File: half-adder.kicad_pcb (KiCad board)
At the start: 2 copper layers, 100 x 100 mm, 55 parts, among them J1 A, J2 B, J3 C, J4 OUTPUT, J5 CARRY OUT, J6 5V, J7 GROUND, Q1 BC547, Q10 BC547, Q11 BC547, Q12 BC547, Q13 BC547, Q14 BC547, Q15 BC547, Q16 BC547, Q17 BC547, Q18 BC547, Q19 BC547, Q2 BC547, Q20 BC547, Q21 BC547, Q22 BC547, Q23 BC547, Q24 BC547, Q25 BC547, Q3 BC547, Q4 BC547, Q5 BC547, Q6 BC547, Q7 BC547, Q8 BC547, Q9 BC547

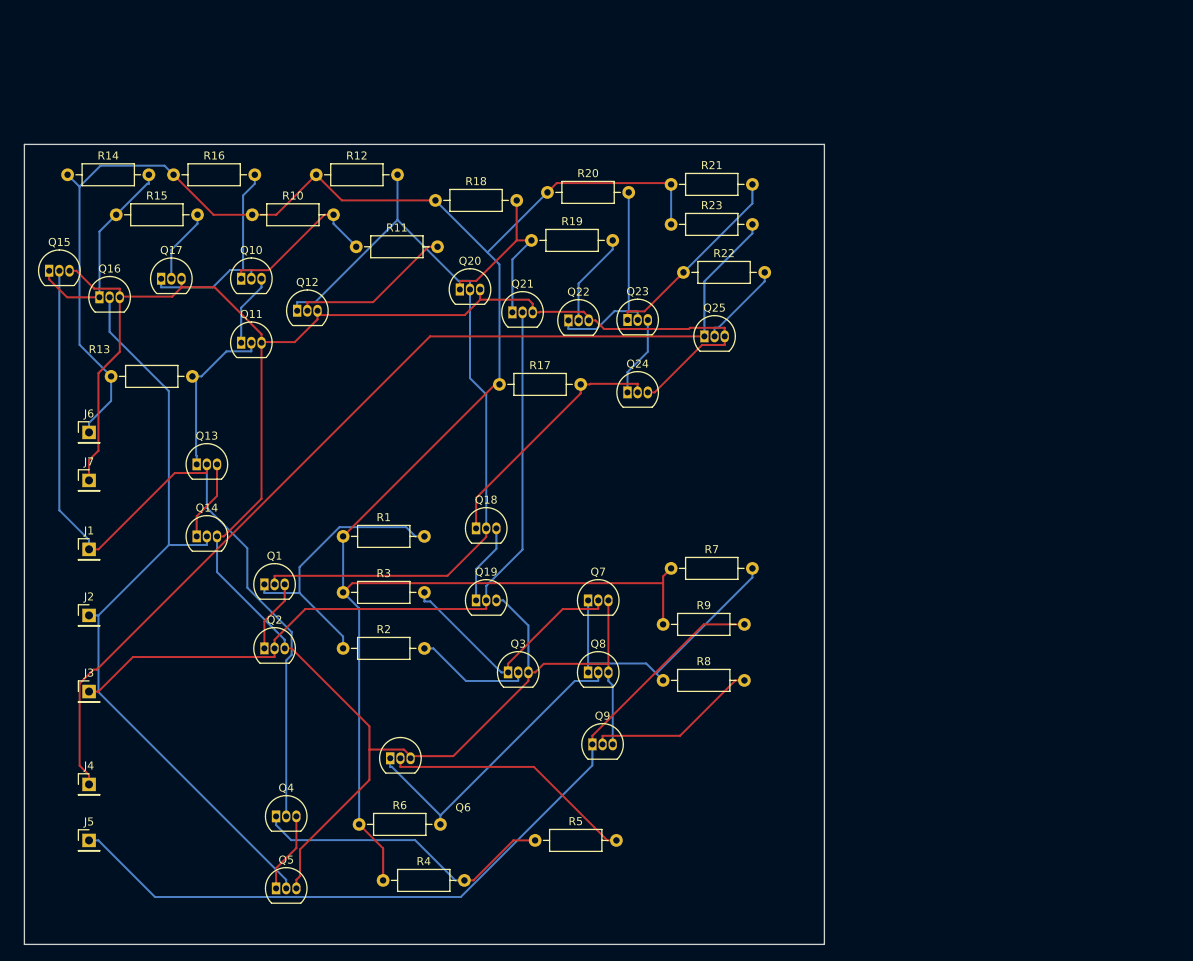
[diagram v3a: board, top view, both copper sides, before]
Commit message: Add ground plane to half adder and modularize or gate
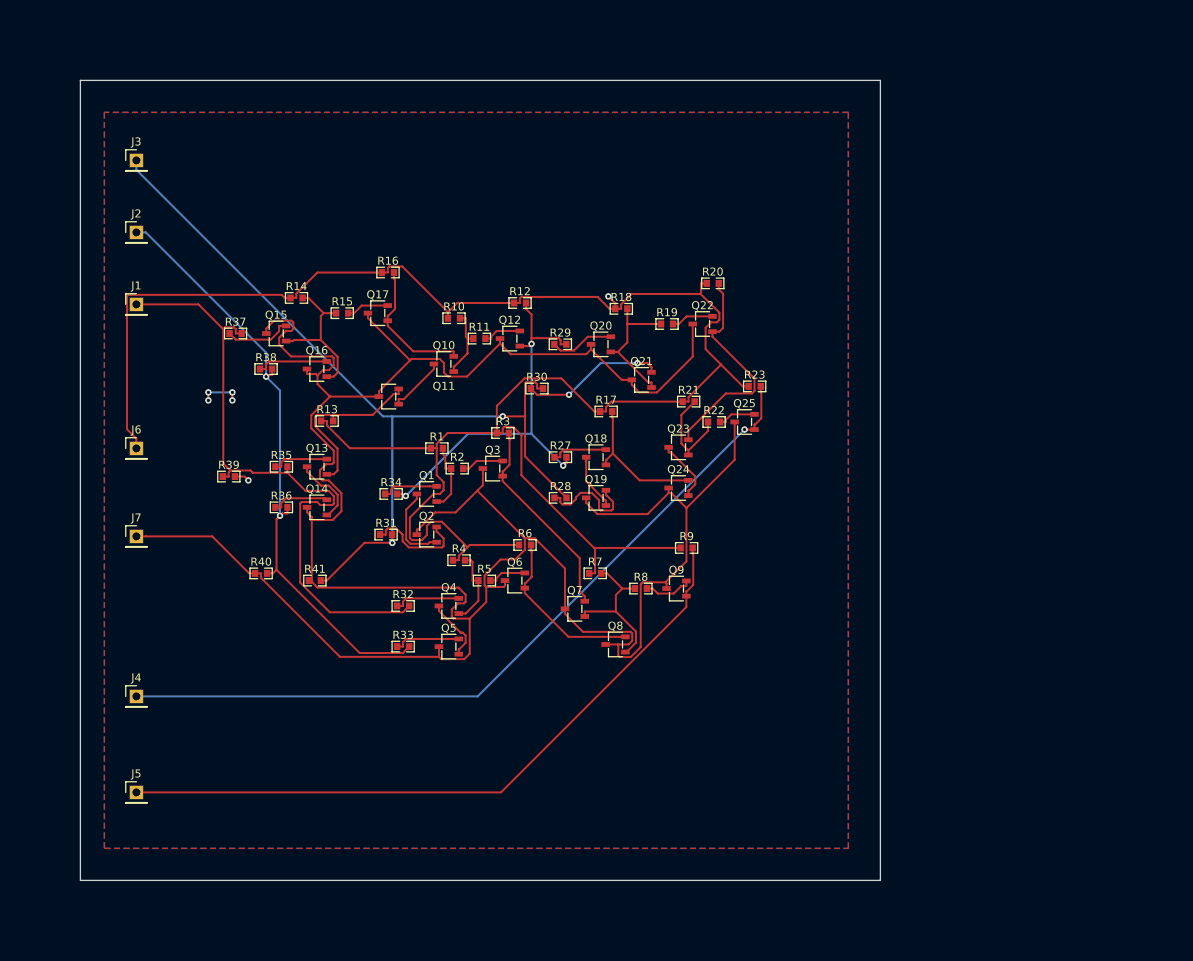
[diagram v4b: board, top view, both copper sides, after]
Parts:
- added R27: 10k, R0603:R0603, F.Cu at (82.0, 68.1)
- added R28: 10k, R0603:R0603, F.Cu at (82.0, 73.2)
- added R29: 10k, R0603:R0603, F.Cu at (82.0, 54.0)
- added R30: 10k, R0603:R0603, F.Cu at (79.1, 59.5)
- added R31: 10k, R0603:R0603, F.Cu at (60.2, 77.8)
- added R32: 10k, R0603:R0603, F.Cu at (62.3, 86.7)
- added R33: 10k, R0603:R0603, F.Cu at (62.3, 91.8)
- added R34: 10k, R0603:R0603, F.Cu at (60.8, 72.7)
- added R35: 10k, R0603:R0603, F.Cu at (47.1, 69.3)
- added R36: 10k, R0603:R0603, F.Cu at (47.1, 74.4)
- added R37: 10k, R0603:R0603, F.Cu at (41.4, 52.6)
- added R38: 10k, R0603:R0603, F.Cu at (45.2, 57.1)
- added R39: 50k, R0603:R0603, F.Cu at (40.6, 70.5)
- added R40: 50k, R0603:R0603, F.Cu at (44.6, 82.6)
- added R41: 50k, R0603:R0603, F.Cu at (51.3, 83.5)
- Q1, Q10, Q11, Q12, Q13, Q14, Q15, Q16, Q17, Q18, Q19, Q2, Q20, Q21, Q22, Q23, Q24, Q25, Q3, Q4, Q5, Q6, Q7, Q8, Q9: value BC547 -> NPN; footprint Package_TO_SOT_THT:TO-92_Inline -> SOT-23-3_L2.9-W1.6-P1.90-LS2.8-BR:SOT-23-3_L2.9-W1.6-P1.90-LS2.8-BR
- R1, R14: value 330 -> 3k; footprint Resistor_THT:R_Axial_DIN0207_L6.3mm_D2.5mm_P10.16mm_Horizontal -> R0603:R0603
- R10, R11, R12, R13, R15, R16, R17, R18, R19, R20, R21, R22, R23, R3, R7, R8, R9: value R -> 3k; footprint Resistor_THT:R_Axial_DIN0207_L6.3mm_D2.5mm_P10.16mm_Horizontal -> R0603:R0603
- R2, R4, R5, R6: value R -> 1k; footprint Resistor_THT:R_Axial_DIN0207_L6.3mm_D2.5mm_P10.16mm_Horizontal -> R0603:R0603
- moved J3 66.7 mm to (29.0, 31.0)
- moved J2 48.2 mm to (29.0, 40.0)
- moved R4 41.1 mm to (69.3, 81.0)
- moved R6 40.6 mm to (77.6, 79.1)
- moved Q5 37.1 mm to (68.1, 91.8)
- moved Q4 34.0 mm to (68.1, 86.7)
- moved R5 33.1 mm to (72.5, 83.5)
- moved R14 32.5 mm to (49.0, 48.2)
- moved J1 31.2 mm to (29.0, 49.0)
- moved R15 30.8 mm to (54.7, 50.1)
- moved R12 30.1 mm to (77.0, 48.8)
- moved R16 29.5 mm to (60.4, 45.0)
- moved Q15 29.4 mm to (46.5, 52.6)
- moved Q16 28.6 mm to (51.6, 57.1)
- moved R10 28.3 mm to (68.7, 50.7)
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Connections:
- net Net-(Q3-C) renamed /ORa
- net Net-(Q6-C) renamed /ORb
- Q12 pad 1: Net-(Q1-B) -> Net-(Q12-C)
- Q13 pad 2: Net-(J1-Pin_1) -> Net-(Q13-B)
- Q14 pad 2: Net-(J2-Pin_1) -> Net-(Q14-B)
- Q15 pad 2: Net-(J1-Pin_1) -> Net-(Q15-B)
- Q16 pad 2: Net-(J2-Pin_1) -> Net-(Q16-B)
- Q18 pad 2: Net-(Q1-B) -> Net-(Q18-B)
- Q19 pad 2: Net-(J3-Pin_1) -> Net-(Q19-B)
- Q2 pad 2: Net-(J3-Pin_1) -> Net-(Q2-B)
- Q20 pad 2: Net-(Q1-B) -> Net-(Q20-B)
- Q21 pad 2: Net-(J3-Pin_1) -> Net-(Q21-B)
- Q4 pad 2: Net-(J1-Pin_1) -> Net-(Q4-B)
- Q5 pad 2: Net-(J2-Pin_1) -> Net-(Q5-B)
- R12 pad 2: Net-(Q1-B) -> Net-(Q12-C)
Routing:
- net Net-(Q1-B): track 98.1 -> 7.15 mm
- net Net-(Q12-C): track 0.00 -> 50.2 mm, vias 0 -> 3
- net GND: track 283.1 -> 331.5 mm, vias 0 -> 1
- net Net-(J4-Pin_1): track 125.6 -> 96.9 mm, vias 0 -> 1
- net Net-(Q4-C): track 38.4 -> 9.73 mm
- net Net-(Q1-C): track 36.0 -> 8.78 mm
- net Net-(Q6-B): track 31.9 -> 4.85 mm
- net Net-(J1-Pin_1): track 104.8 -> 80.6 mm
- net Net-(J2-Pin_1): track 97.3 -> 76.5 mm, vias 0 -> 2
- net Net-(Q7-C): track 37.4 -> 19.5 mm
- net Net-(Q21-B): track 0.00 -> 17.9 mm, vias 0 -> 2
- net /ORb: track 38.7 -> 21.3 mm
- net Net-(J3-Pin_1): track 94.1 -> 109.6 mm, vias 0 -> 2
- net Net-(Q9-B): track 21.7 -> 6.21 mm
- net Net-(Q12-B): track 20.2 -> 4.85 mm
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- added copper zone on F.Cu, net +5V
- added copper zone on B.Cu, net GND
